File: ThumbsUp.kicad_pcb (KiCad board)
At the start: 2 copper layers, 250.8 x 280.8 mm, 169 parts, among them IC1 RP2040, IC2 W25Q128JVSIM, IC3 RP2040, IC4 W25Q128JVSIM, J1 Conn_01x04_Male, J10 Raiser_Male, J11 Raiser_Female, J12 Raiser_Male, J13 Raiser_Female, J14 Raiser_Male, J15 Raiser_Female, J16 Raiser_Male, J17 Raiser_Female, J18 Raiser_Male, J19 Raiser_Female, J2 Conn_01x04_Male, J20 Conn_01x04_Female, J21 Conn_01x04_Female, J22 Conn_01x04_Female, J23 Conn_01x04_Female, J24 Conn_01x04_Male, J25 Conn_01x04_Male, J26 Conn_01x04_Male, J27 Conn_01x04_Male, J28 Conn_01x04_Female, J29 Conn_01x04_Female, J3 Conn_01x04_Female, J30 Conn_01x04_Female, J31 Conn_01x04_Female, J32 USB_C_Receptacle_USB2.0, J33 Raiser_Male, J34 Raiser_Female, J35 Raiser_Male, J36 STX-3501-3N, J37 USB_C_Receptacle_USB2.0, J38 Raiser_Female, J39 Raiser_Male, J4 Conn_01x04_Male, J40 Raiser_Female, J41 Raiser_Male, J42 Raiser_Female, J43 Raiser_Male, J44 Raiser_Female, J45 Raiser_Male, J46 STX-3501-3N, J47 Raiser_Female, J48 Raiser_Male, J49 Raiser_Female, J5 Conn_01x04_Female, J50 Raiser_Male, J51 Raiser_Female, J52 Raiser_Male, J6 Conn_01x04_Male, J7 Conn_01x04_Male, J8 Conn_01x04_Male, J9 Raiser_Female, U1 NCP1117-3.3_SOT223, U2 NCP1117-3.3_SOT223, Y1 ABLS-12.000MHZ-B4-T, Y2 ABLS-12.000MHZ-B4-T

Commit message: Put the screensilk back on
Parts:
- added G***: LOGO, Silkscreens:Crowfeet75, F.Cu at (151.6, 565.1)
- added G***: LOGO, Silkscreens:Crowfeet75, B.Cu at (140.8, 562.8)
- added G***: LOGO, Silkscreens:Crowfeet75, F.Cu at (154.6, 398.7)
- moved J10 10.6 mm to (93.5, 349.5)
- moved J14 10.6 mm to (132.2, 346.0)
- moved J18 10.6 mm to (119.6, 335.5)
- moved J33 10.6 mm to (195.3, 349.3)
- moved J35 10.6 mm to (169.1, 335.4)
- moved J4 10.6 mm to (98.7, 357.2)
- moved J48 10.6 mm to (156.6, 345.9)
- moved J6 10.6 mm to (190.3, 357.0)
- moved MX18 10.6 mm to (121.6, 347.4)
- moved MX22 10.6 mm to (102.5, 347.4)
- moved MX26 10.6 mm to (186.4, 347.4)
- moved MX30 10.6 mm to (167.3, 347.4)
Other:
- board size 250.8 x 280.8 mm -> 250.8 x 270.5 mm

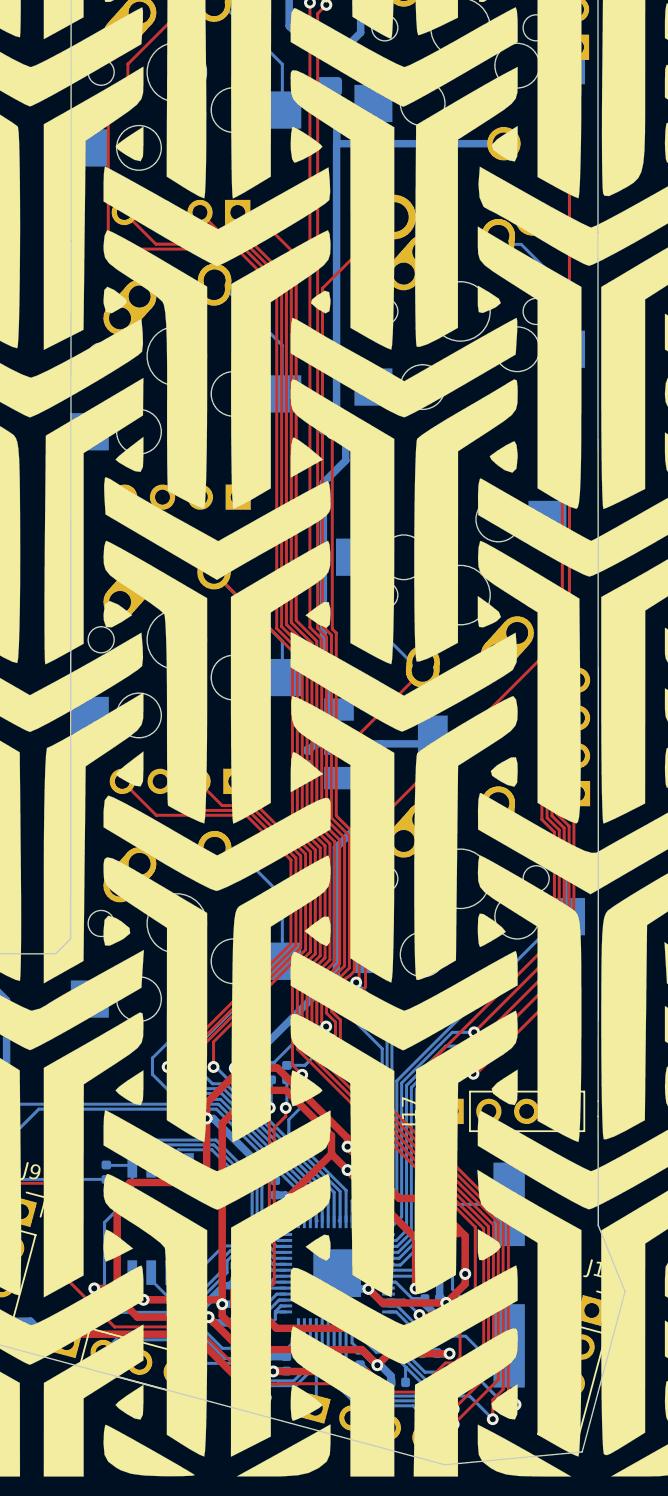
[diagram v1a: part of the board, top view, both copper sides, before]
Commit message: Moved tracks of K_5 away from K_E, K4 from K_GRAVE to avoid short circuits in some of the board copies.
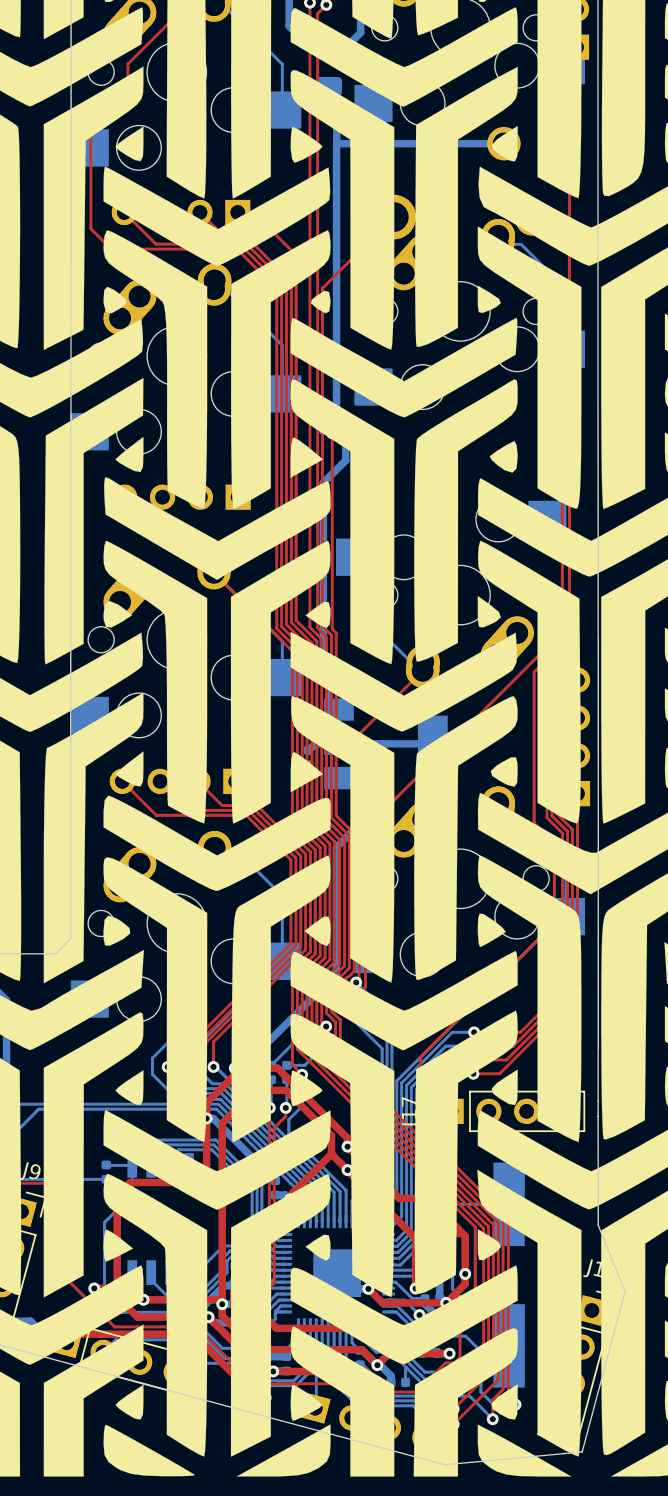
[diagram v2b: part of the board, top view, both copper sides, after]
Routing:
- net K_E: track 44.0 -> 46.0 mm
- net K_W: track 42.4 -> 44.2 mm
- net K_4: track 124.0 -> 125.5 mm
- net K_Q: track 40.6 -> 42.1 mm
- net K_ESC: track 38.2 -> 39.1 mm
- net K_5: track 121.9 -> 122.8 mm

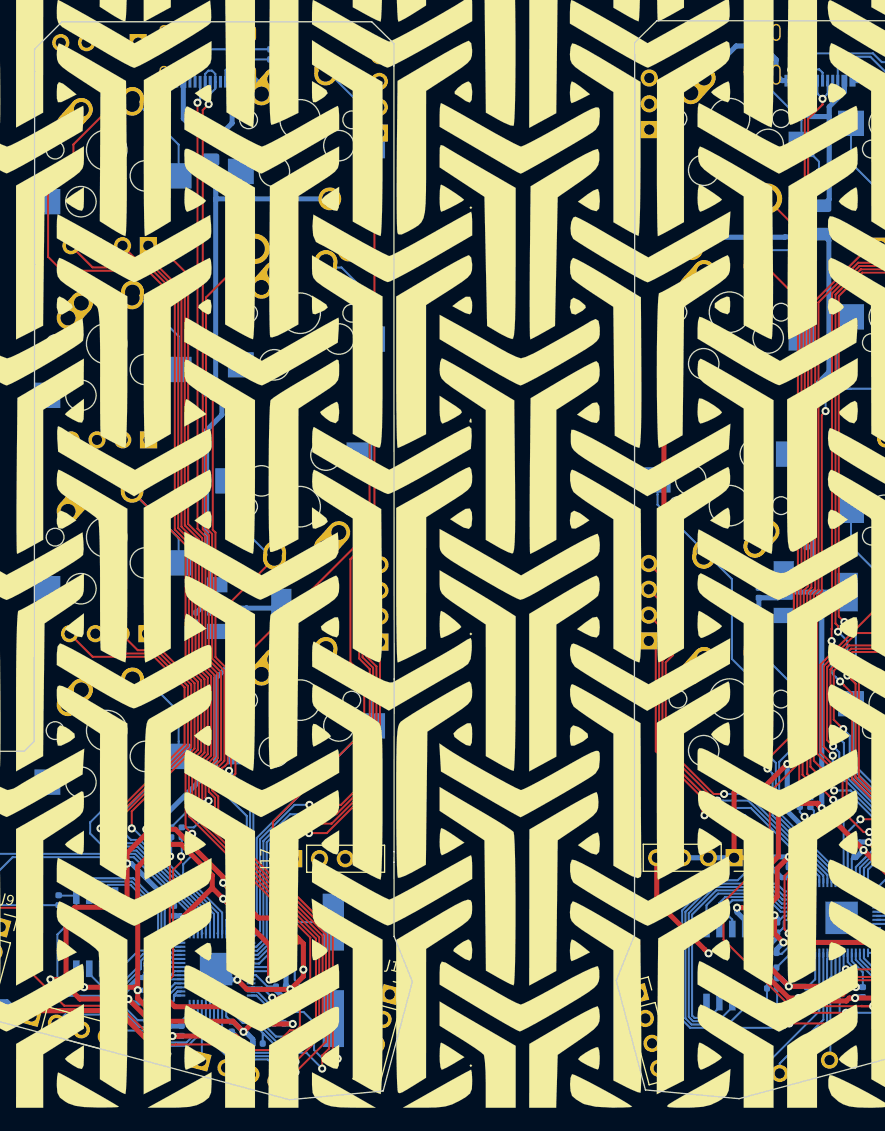
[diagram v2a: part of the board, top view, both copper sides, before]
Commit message: Left L2 - straightened the USB signal lines.
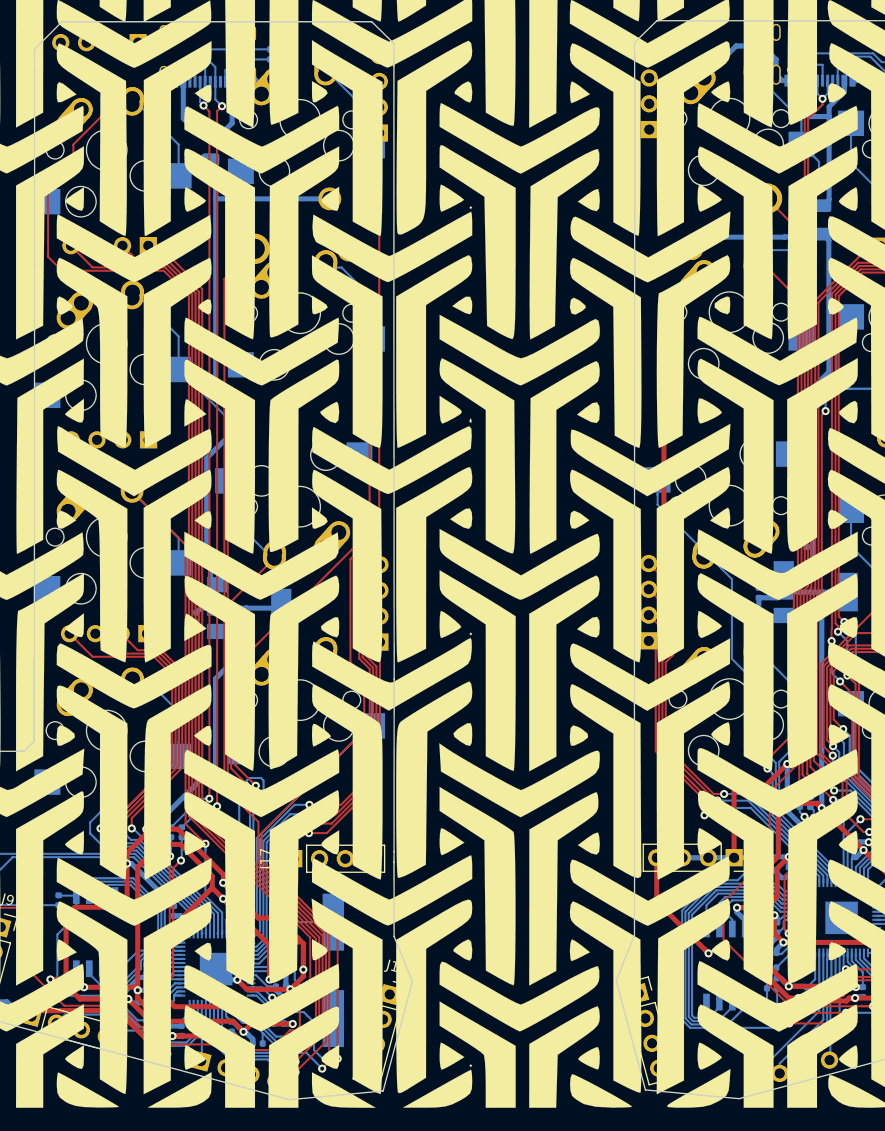
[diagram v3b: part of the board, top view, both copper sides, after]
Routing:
- net K_G: track 49.9 -> 52.7 mm
- net L-TIP: track 102.1 -> 99.6 mm
- net K_F: track 57.9 -> 56.2 mm
- net L-RING1: track 106.4 -> 108.0 mm
- net D-: track 80.0 -> 78.5 mm
- net K_R: track 70.5 -> 69.2 mm
- net RD-: track 73.9 -> 75.2 mm
- net K_T: track 86.2 -> 85.0 mm
- net K_Z: track 40.6 -> 39.6 mm
- net K_3: track 103.5 -> 102.5 mm
- net K_LCTL: track 37.9 -> 36.9 mm
- net K_X: track 43.5 -> 42.5 mm
- net K_5: track 122.8 -> 123.7 mm
- net K_C: track 46.5 -> 45.8 mm
